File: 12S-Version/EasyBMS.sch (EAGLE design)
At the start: 145 parts, among them IC1 LTC6811IG-2#PBF, Q10 BSS84LT1G, Q11 BSS84LT1G, Q12 BSS84LT1G, Q13 BSS84LT1G, Q2 BSS84LT1G, Q3 BSS84LT1G, Q4 BSS84LT1G, Q5 BSS84LT1G, Q6 BSS84LT1G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

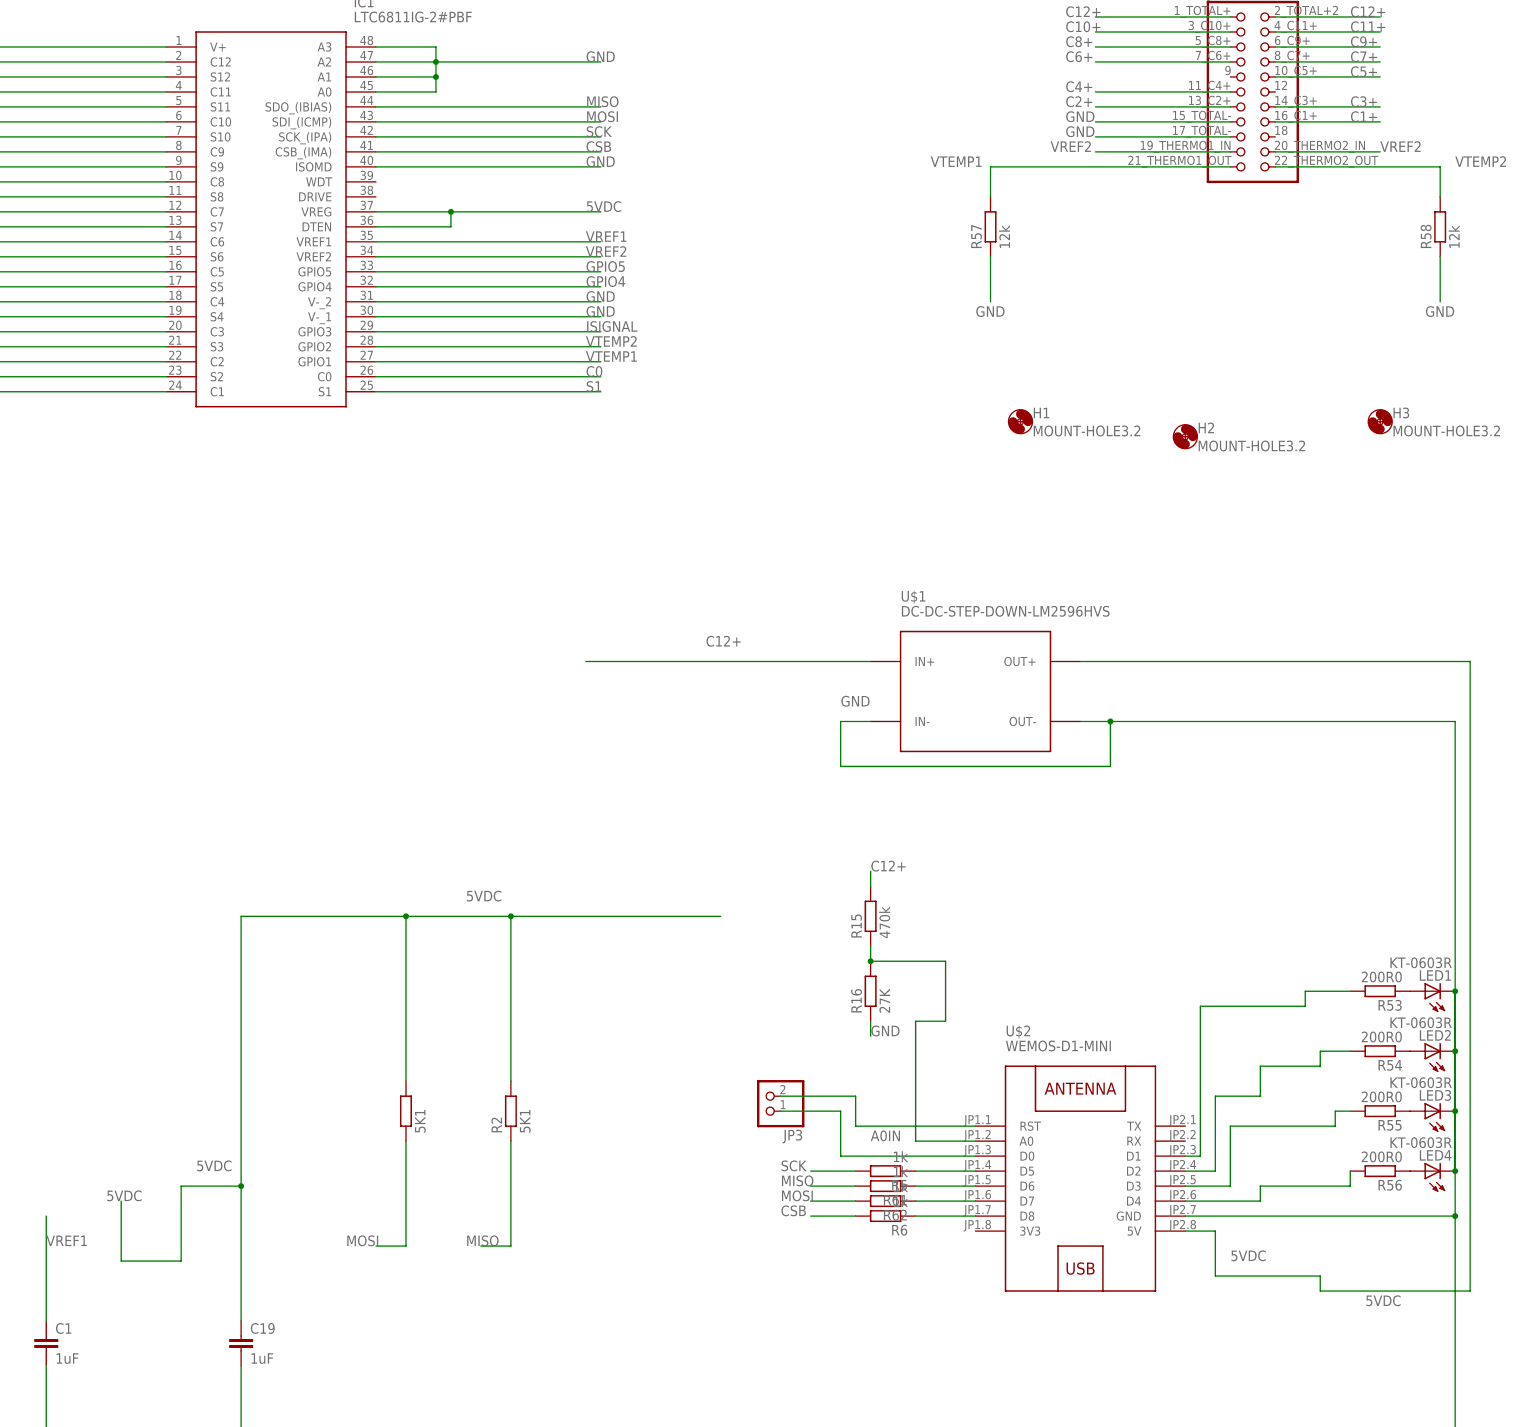
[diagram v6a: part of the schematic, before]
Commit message: Bugfix of SPI MISO pullup and Bat C1- connection
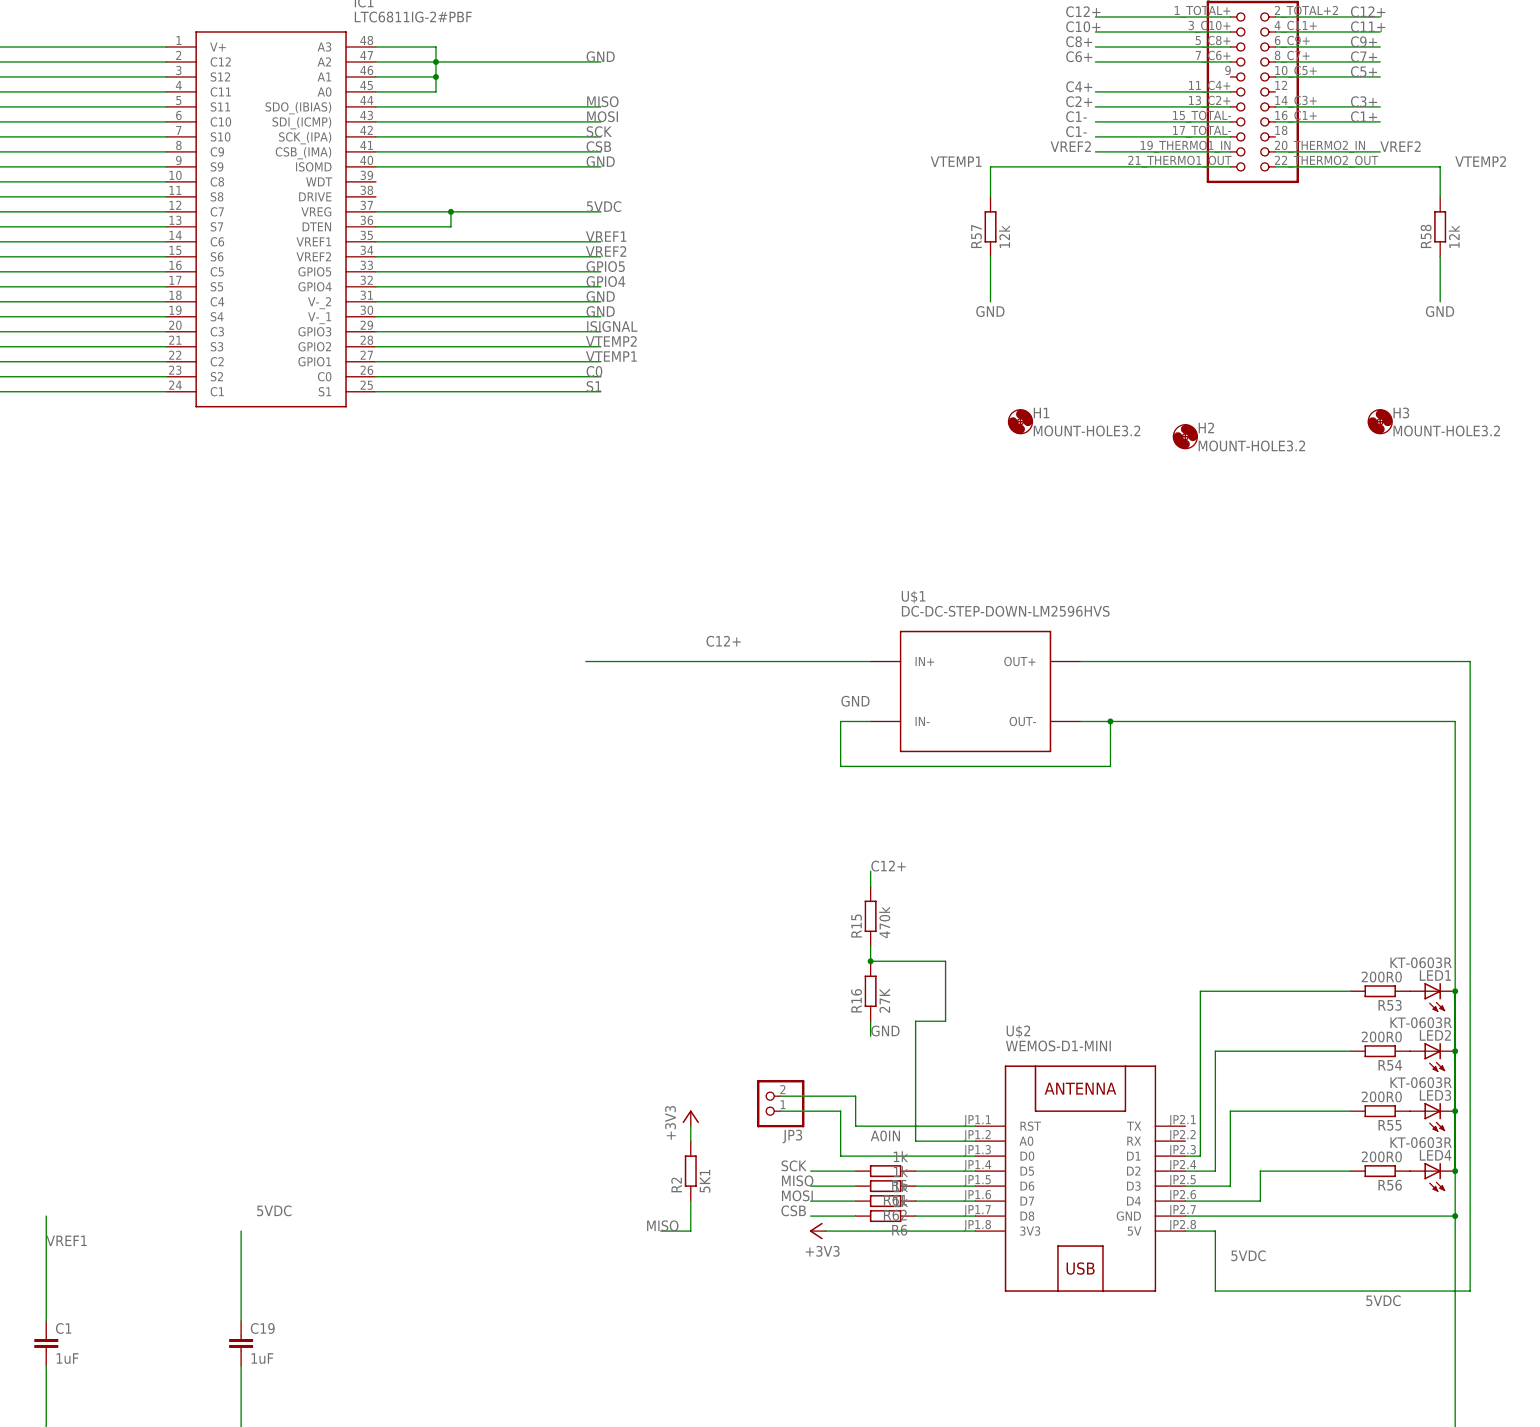
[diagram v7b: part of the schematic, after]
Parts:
- removed R1: 5K1, rcl:R-EU_R0603
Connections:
- new net +3V3: R2.2, U$2.3V3
- net 5VDC: no longer R1.2, R2.2
- net C1-: now also JP7.15_TOTAL-, JP7.TOTAL-
- net GND: no longer JP7.15_TOTAL-, JP7.TOTAL-
- net MOSI: no longer R1.1
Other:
- moved on the sheet: R2

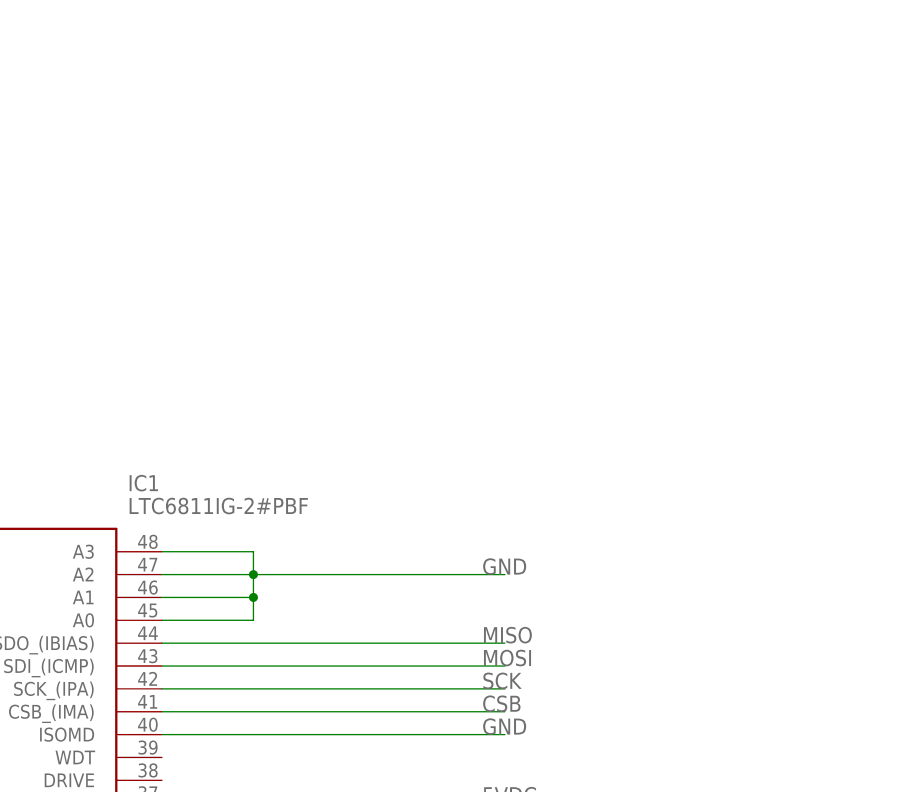
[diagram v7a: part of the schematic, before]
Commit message: new branch for LTC68xx-1 chip, small changes on base board
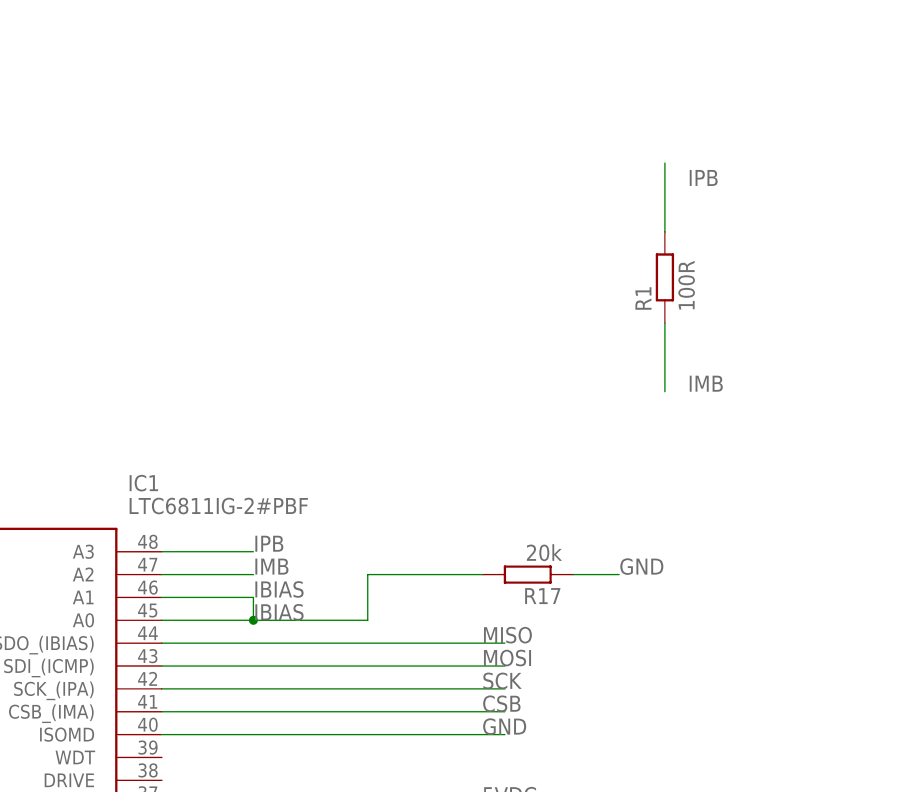
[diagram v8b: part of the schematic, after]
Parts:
- added R1: 100R, rcl:R-EU_R0603
- added R17: 20k, rcl:R-EU_R0603
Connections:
- new net IBIAS: IC1.A0, IC1.A1, R17.2
- new net IMB: IC1.A2, R1.1
- new net IPB: IC1.A3, R1.2
- net GND: now also R17.1; no longer IC1.A0, IC1.A1, IC1.A2, IC1.A3
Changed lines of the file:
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@@
 <part name="+3V1" library="supply1" library_urn="urn:adsk.eagle:library:371" deviceset="+3V3" device=""/>
 <part name="+3V2" library="supply1" library_urn="urn:adsk.eagle:library:371" deviceset="+3V3" device=""/>
+<part name="R1" library="rcl" library_urn="urn:adsk.eagle:library:334" deviceset="R-EU_" device="R0603" package3d_urn="urn:adsk.eagle:package:23555/2" value="100R"/>
+<part name="R17" library="rcl" library_urn="urn:adsk.eagle:library:334" deviceset="R-EU_" device="R0603" package3d_urn="urn:adsk.eagle:package:23555/2" value="20k"/>
 </parts>
 <sheets>
@@
 <instance part="+3V2" gate="G$1" x="83.82" y="309.88" smashed="yes" rot="R90">
 <attribute name="VALUE" x="88.9" y="307.34" size="1.778" layer="96" rot="R180"/>
+</instance>
+<instance part="R1" gate="G$1" x="66.04" y="541.02" smashed="yes" rot="R90">
+<attribute name="NAME" x="64.5414" y="537.21" size="1.778" layer="95" rot="R90"/>
+<attribute name="VALUE" x="69.342" y="537.21" size="1.778" layer="96" rot="R90"/>
+</instance>
+<instance part="R17" gate="G$1" x="50.8" y="508" smashed="yes" rot="R180">
+<attribute name="NAME" x="54.61" y="506.5014" size="1.778" layer="95" rot="R180"/>
+<attribute name="VALUE" x="54.61" y="511.302" size="1.778" layer="96" rot="R180"/>
 </instance>
 </instances>
@@
 </segment>
 <segment>
-<pinref part="IC1" gate="G$1" pin="A3"/>
-<wire x1="10.16" y1="510.54" x2="20.32" y2="510.54" width="0.1524" layer="91"/>
-<wire x1="20.32" y1="510.54" x2="20.32" y2="508" width="0.1524" layer="91"/>
-<pinref part="IC1" gate="G$1" pin="A2"/>
-<wire x1="20.32" y1="508" x2="10.16" y2="508" width="0.1524" layer="91"/>
-<pinref part="IC1" gate="G$1" pin="A1"/>
-<wire x1="10.16" y1="505.46" x2="20.32" y2="505.46" width="0.1524" layer="91"/>
-<wire x1="20.32" y1="505.46" x2="20.32" y2="508" width="0.1524" layer="91"/>
-<junction x="20.32" y="508"/>
-<pinref part="IC1" gate="G$1" pin="A0"/>
-<wire x1="10.16" y1="502.92" x2="20.32" y2="502.92" width="0.1524" layer="91"/>
-<wire x1="20.32" y1="502.92" x2="20.32" y2="505.46" width="0.1524" layer="91"/>
-<junction x="20.32" y="505.46"/>
-<wire x1="20.32" y1="508" x2="48.26" y2="508" width="0.1524" layer="91"/>
-<label x="45.72" y="508" size="1.778" layer="95"/>
-</segment>
-<segment>
 <pinref part="C5" gate="G$1" pin="2"/>
 <wire x1="-182.88" y1="68.58" x2="-182.88" y2="66.04" width="0.1524" layer="91"/>
@@
 <label x="-180.34" y="63.5" size="1.778" layer="95"/>
 <pinref part="R13" gate="G$1" pin="2"/>
+</segment>
+<segment>
+<pinref part="R17" gate="G$1" pin="1"/>
+<wire x1="55.88" y1="508" x2="60.96" y2="508" width="0.1524" layer="91"/>
+<label x="60.96" y="508" size="1.778" layer="95"/>
 </segment>
 </net>
@@
 </segment>
 </net>
+<net name="IPB" class="0">
+<segment>
+<pinref part="IC1" gate="G$1" pin="A3"/>
+<wire x1="10.16" y1="510.54" x2="20.32" y2="510.54" width="0.1524" layer="91"/>
+<label x="20.32" y="510.54" size="1.778" layer="95"/>
+</segment>
+<segment>
+<wire x1="66.04" y1="553.72" x2="66.04" y2="546.1" width="0.1524" layer="91"/>
+<pinref part="R1" gate="G$1" pin="2"/>
+<label x="68.58" y="551.18" size="1.778" layer="95"/>
+</segment>
+</net>
+<net name="IMB" class="0">
+<segment>
+<pinref part="IC1" gate="G$1" pin="A2"/>
+<wire x1="10.16" y1="508" x2="20.32" y2="508" width="0.1524" layer="91"/>
+<label x="20.32" y="508" size="1.778" layer="95"/>
+</segment>
+<segment>
+<pinref part="R1" gate="G$1" pin="1"/>
+<wire x1="66.04" y1="535.94" x2="66.04" y2="528.32" width="0.1524" layer="91"/>
+<label x="68.58" y="528.32" size="1.778" layer="95"/>
+</segment>
+</net>
+<net name="IBIAS" class="0">
+<segment>
+<pinref part="IC1" gate="G$1" pin="A1"/>
+<wire x1="10.16" y1="505.46" x2="20.32" y2="505.46" width="0.1524" layer="91"/>
+<label x="20.32" y="505.46" size="1.778" layer="95"/>
+<pinref part="IC1" gate="G$1" pin="A0"/>
+<wire x1="10.16" y1="502.92" x2="20.32" y2="502.92" width="0.1524" layer="91"/>
+<label x="20.32" y="502.92" size="1.778" layer="95"/>
+<wire x1="20.32" y1="505.46" x2="20.32" y2="502.92" width="0.1524" layer="91"/>
+<wire x1="20.32" y1="502.92" x2="33.02" y2="502.92" width="0.1524" layer="91"/>
+<wire x1="33.02" y1="502.92" x2="33.02" y2="508" width="0.1524" layer="91"/>
+<junction x="20.32" y="502.92"/>
+<wire x1="33.02" y1="508" x2="45.72" y2="508" width="0.1524" layer="91"/>
+<pinref part="R17" gate="G$1" pin="2"/>
+</segment>
+</net>
